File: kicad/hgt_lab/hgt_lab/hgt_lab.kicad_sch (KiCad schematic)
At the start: 10 parts

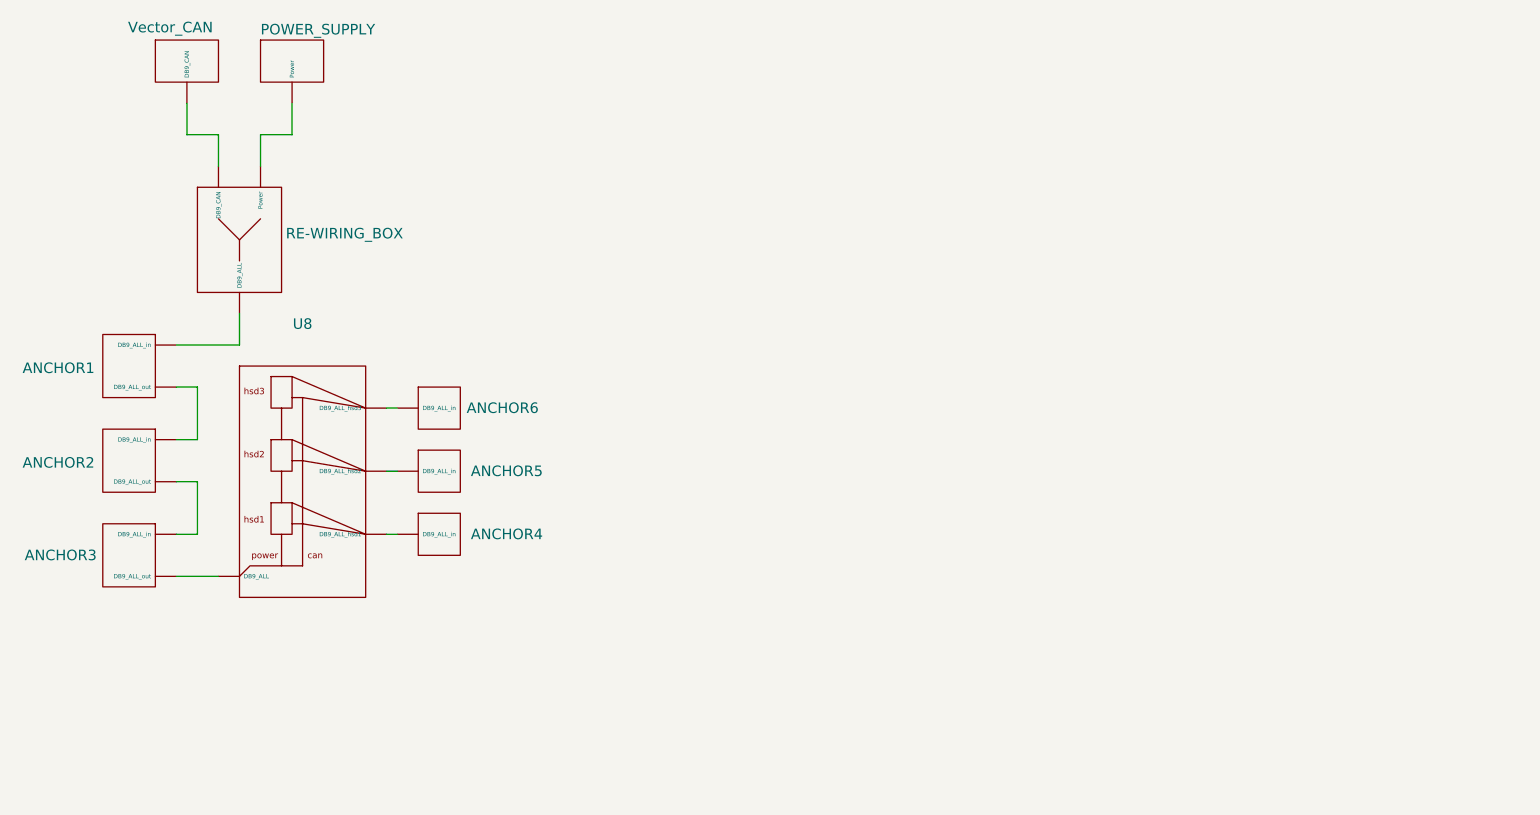
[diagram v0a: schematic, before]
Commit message: add annotation for hgt_lab schematic
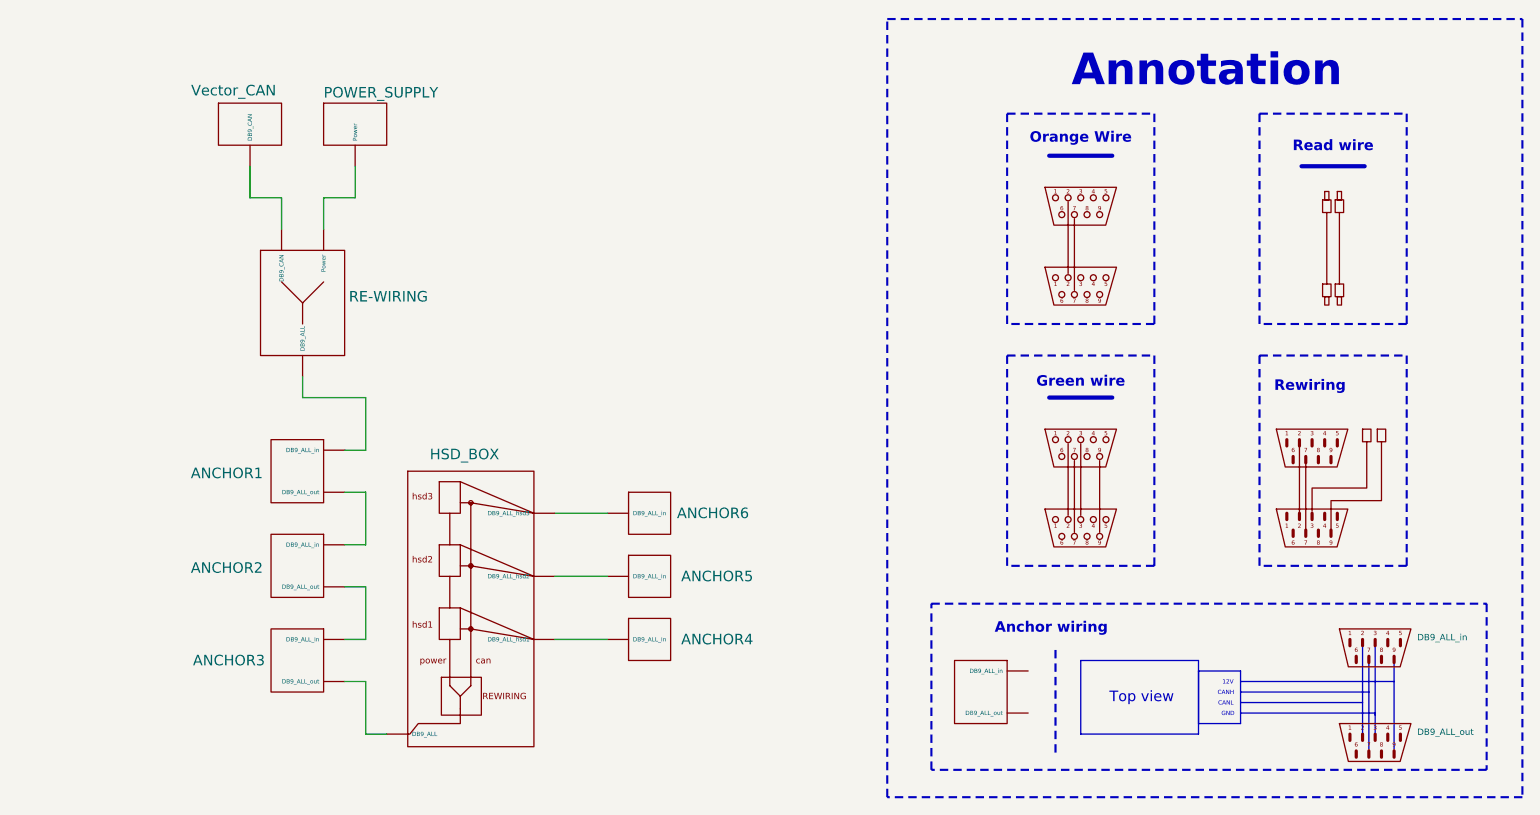
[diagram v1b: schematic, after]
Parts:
- added ANCHOR: ~, symbol hgt_lab:anchor_daisy_chain
- added DB9_ALL_in, DB9_ALL_out: ~, symbol hgt_lab:DB9_male
- added U1: ~, symbol hgt_lab:DB9_ALL_cable
- added U2: ~, symbol hgt_lab:DB9_CAN_cable
- added U3: ~, symbol hgt_lab:Power_cable
- added U4: ~, symbol hgt_lab:rewiring_cable
- renumbered U8 to HSD_BOX, RE-WIRING_BOX to RE-WIRING
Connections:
- net at ANCHOR2. (DB9_ALL_out): now also ANCHOR3. (DB9_ALL_out); no longer ANCHOR1. (DB9_ALL_out)
- net at ANCHOR3. (DB9_ALL_out): now also HSD_BOX. (DB9_ALL_hsd1); no longer ANCHOR2. (DB9_ALL_out)
- new net: ANCHOR1. (DB9_ALL_out), ANCHOR2. (DB9_ALL_out)
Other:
- note added: "12V"
- note added: "Anchor wiring"
- note added: "Annotation"
- note added: "CANH"
- note added: "CANL"
- note added: "GND"
- note added: "Green wire"
- note added: "Orange Wire"
- note added: "Read wire"
- note added: "Rewiring"
- note added: "Top view"
- moved on the sheet: ANCHOR1, ANCHOR2, ANCHOR3, ANCHOR4, ANCHOR5, ANCHOR6, POWER_SUPPLY, RE-WIRING, Vector_CAN

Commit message: update schematic and generate the pdf file
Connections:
- net at ANCHOR2. (DB9_ALL_out): now also ANCHOR3. (DB9_ALL_out); no longer ANCHOR1. (DB9_ALL_out)
- net at ANCHOR3. (DB9_ALL_out): now also HSD_BOX. (DB9_ALL_hsd1); no longer ANCHOR2. (DB9_ALL_out)
- new net: ANCHOR1. (DB9_ALL_out), ANCHOR2. (DB9_ALL_out)

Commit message: update hgt_lab
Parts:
- removed RE-WIRING: ~, symbol hgt_lab:can_power_rewrire_box
- added REWIRING: ~, symbol hgt_lab:can_power_rewrire
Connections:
- net at ANCHOR2. (DB9_ALL_out): now also ANCHOR3. (DB9_ALL_out); no longer ANCHOR1. (DB9_ALL_out)
- net at ANCHOR3. (DB9_ALL_out): now also HSD_BOX. (DB9_ALL_hsd1); no longer ANCHOR2. (DB9_ALL_out)
- net at Vector_CAN. (DB9_CAN): now also REWIRING. (Power)
- net at ANCHOR5. (DB9_ALL_in): no longer HSD_BOX. (DB9_ALL_hsd1)
- net at ANCHOR6. (DB9_ALL_in): no longer HSD_BOX. (DB9_ALL_hsd1)
- net at ANCHOR4. (DB9_ALL_in): no longer HSD_BOX. (DB9_ALL_hsd1)
- net at POWER_SUPPLY. (Power): now also REWIRING. (Power)
- net at ANCHOR1. (DB9_ALL_out): now also REWIRING. (Power)
- new net: ANCHOR1. (DB9_ALL_out), ANCHOR2. (DB9_ALL_out)
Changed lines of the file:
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@@
+	)
+	(symbol
+		(lib_id "hgt_lab:can_power_rewrire")
+		(at 46.99 48.26 0)
+		(unit 1)
+		(exclude_from_sim no)
+		(in_bom yes)
+		(on_board yes)
+		(dnp no)
+		(fields_autoplaced yes)
+		(property "Reference" "REWIRING"
+			(at 53.34 48.2599 0)
+			(effects
+				(font
+					(size 1.27 1.27)
+				)
+				(justify left)
+			)
+		)
+		(property "Value" "~"
+			(at 53.34 50.7999 0)
+			(effects
+				(font
+					(size 1.27 1.27)
+				)
+				(justify left)
+				(hide yes)
+			)
+		)
+		(property "Footprint" ""
+			(at 46.99 48.26 0)
+			(effects
+				(font
+					(size 1.27 1.27)
+				)
+				(hide yes)
+			)
+		)
+		(property "Datasheet" ""
+			(at 46.99 48.26 0)
+			(effects
+				(font
+					(size 1.27 1.27)
+				)
+				(hide yes)
+			)
+		)
+		(property "Description" ""
+			(at 46.99 48.26 0)
+			(effects
+				(font
+					(size 1.27 1.27)
+				)
+				(hide yes)
+			)
+		)
+		(pin ""
+		)
+		(pin ""
+		)
+		(pin ""
+		)
+		(instances
+			(project ""
+				(path "/71882b24-4576-410d-80ea-9cc90d8a026f"
+					(reference "REWIRING")
+					(unit 1)
+				)
+			)
+		)
 	)
 	(symbol
@@
 					(unit 1)
 				)
-			)
-		)
-	)
-	(symbol
-		(lib_id "hgt_lab:can_power_rewrire_box")
-		(at 46.99 48.26 0)
-		(unit 1)
-		(exclude_from_sim no)
-		(in_bom yes)
-		(on_board yes)
-		(dnp no)
-		(property "Reference" "RE-WIRING"
-			(at 52.578 48.768 0)
-			(effects
-				(font
-					(size 1.27 1.27)
-				)
-				(justify left)
-			)
-		)
-		(property "Value" "~"
-			(at 53.34 50.7999 0)
-			(effects
-				(font
-					(size 1.27 1.27)
-				)
-				(justify left)
-				(hide yes)
-			)
-		)
-		(property "Footprint" ""
-			(at 46.99 48.26 0)
-			(effects
-				(font
-					(size 1.27 1.27)
-				)
-				(hide yes)
-			)
-		)
-		(property "Datasheet" ""
-			(at 46.99 48.26 0)
-			(effects
-				(font
-					(size 1.27 1.27)
-				)
-				(hide yes)
-			)
-		)
-		(property "Description" ""
-			(at 46.99 48.26 0)
-			(effects
-				(font
-					(size 1.27 1.27)
-				)
-				(hide yes)
-			)
-		)
-		(pin ""
-		)
-		(pin ""
-		)
-		(pin ""
-		)
-		(instances
-			(project ""
-				(path "/71882b24-4576-410d-80ea-9cc90d8a026f"
-					(reference "RE-WIRING")
-					(unit 1)
-				)
